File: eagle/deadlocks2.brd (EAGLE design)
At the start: 18 parts, among them J1 6_PIN_SERIAL_CABLEPTH, U1 328P

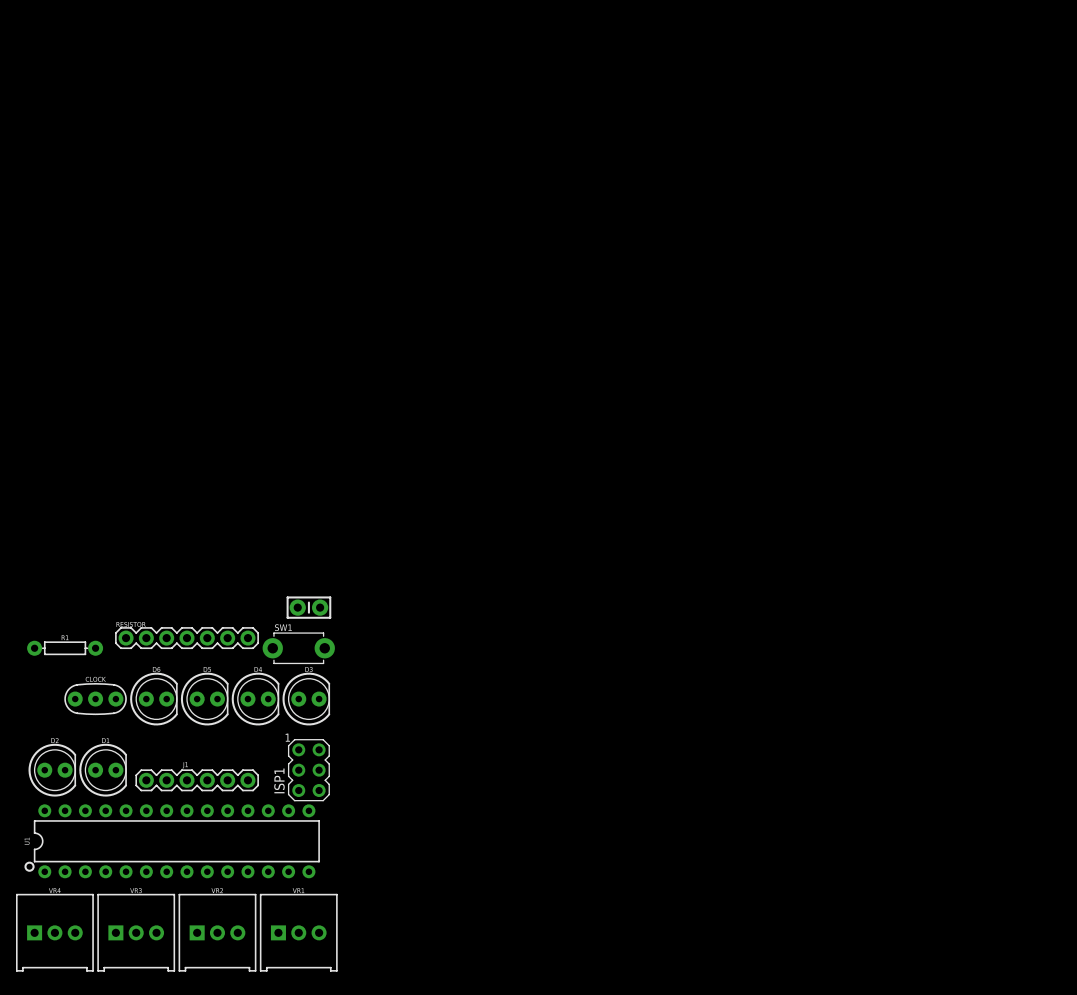
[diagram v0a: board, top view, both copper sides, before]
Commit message: Updates to BOM, board design, and datasheets.
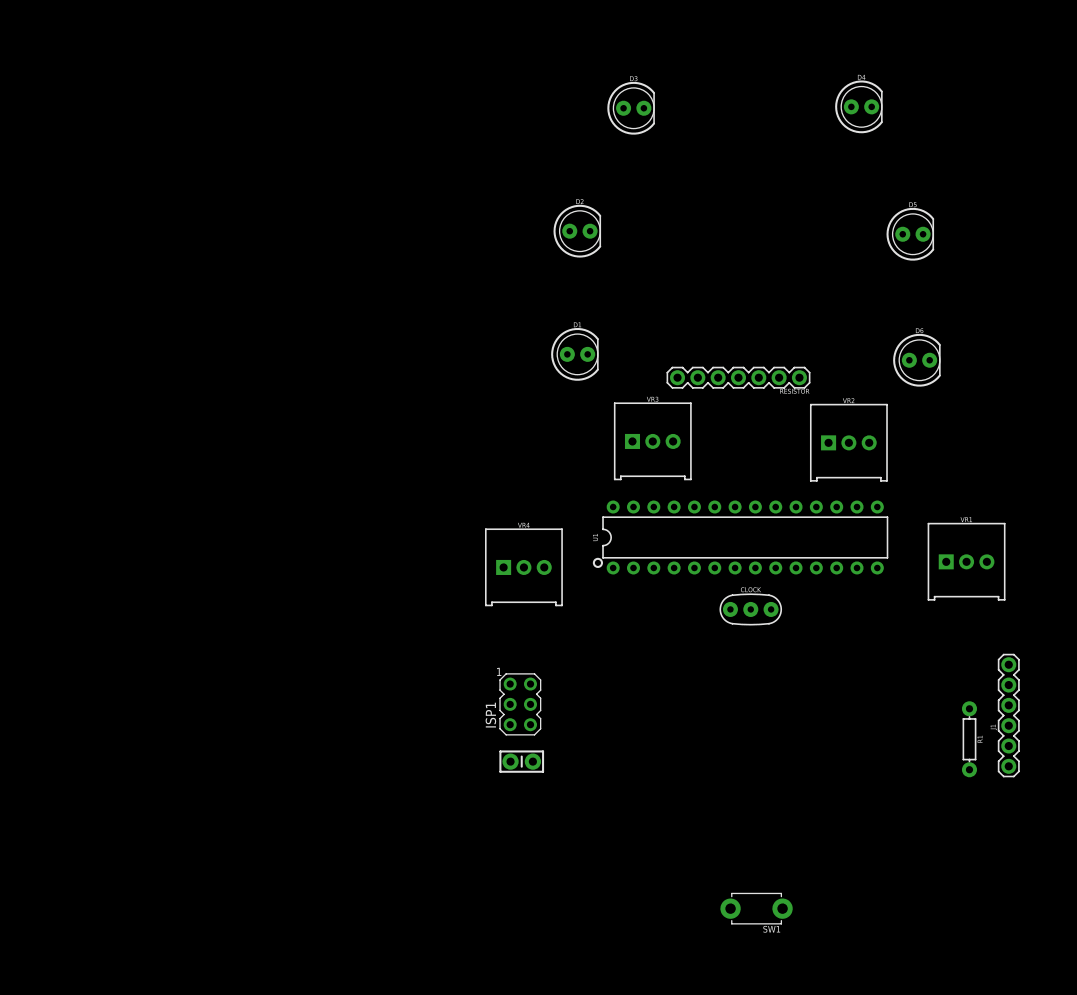
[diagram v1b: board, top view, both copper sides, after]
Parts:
- moved R1 113.6 mm to (66.1, 30.5), turned to 270 degrees
- moved J1 107.8 mm to (71.0, 27.1), turned to 90 degrees
- moved D4 105.7 mm to (52.6, 109.6)
- moved D5 105.6 mm to (59.0, 93.7)
- moved D6 104.4 mm to (59.8, 77.9)
- moved VR2 99.9 mm to (51.0, 67.6)
- moved VR1 95.5 mm to (65.7, 52.7)
- moved D2 94.1 mm to (17.4, 94.0)
- moved RESISTOR 90.2 mm to (44.8, 75.7), turned to 180 degrees
- moved VR3 89.1 mm to (26.5, 67.8)
- moved D3 84.3 mm to (24.1, 109.4)
- moved CLOCK 82.7 mm to (38.7, 46.8)
- moved U1 80.6 mm to (38.0, 55.8)
- moved D1 78.6 mm to (17.1, 78.6)
- moved VR4 74.3 mm to (10.4, 52.0)
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
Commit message: Updated board
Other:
- board outline added: 78.4 x 120.2 mm
- board text removed: "/home/thedevilsvoice/workspace/dead10c5_2018/art/DE:AD:10:C5-2.bmp"
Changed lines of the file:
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@@
 <layer number="27" name="tValues" color="7" fill="1" visible="yes" active="yes"/>
 <layer number="28" name="bValues" color="7" fill="1" visible="yes" active="yes"/>
-<layer number="29" name="tStop" color="7" fill="3" visible="no" active="yes"/>
-<layer number="30" name="bStop" color="7" fill="6" visible="no" active="yes"/>
-<layer number="31" name="tCream" color="7" fill="4" visible="no" active="yes"/>
-<layer number="32" name="bCream" color="7" fill="5" visible="no" active="yes"/>
-<layer number="33" name="tFinish" color="6" fill="3" visible="no" active="yes"/>
-<layer number="34" name="bFinish" color="6" fill="6" visible="no" active="yes"/>
-<layer number="35" name="tGlue" color="7" fill="4" visible="no" active="yes"/>
-<layer number="36" name="bGlue" color="7" fill="5" visible="no" active="yes"/>
-<layer number="37" name="tTest" color="7" fill="1" visible="no" active="yes"/>
-<layer number="38" name="bTest" color="7" fill="1" visible="no" active="yes"/>
+<layer number="29" name="tStop" color="7" fill="3" visible="yes" active="yes"/>
+<layer number="30" name="bStop" color="7" fill="6" visible="yes" active="yes"/>
+<layer number="31" name="tCream" color="7" fill="4" visible="yes" active="yes"/>
+<layer number="32" name="bCream" color="7" fill="5" visible="yes" active="yes"/>
+<layer number="33" name="tFinish" color="6" fill="3" visible="yes" active="yes"/>
+<layer number="34" name="bFinish" color="6" fill="6" visible="yes" active="yes"/>
+<layer number="35" name="tGlue" color="7" fill="4" visible="yes" active="yes"/>
+<layer number="36" name="bGlue" color="7" fill="5" visible="yes" active="yes"/>
+<layer number="37" name="tTest" color="7" fill="1" visible="yes" active="yes"/>
+<layer number="38" name="bTest" color="7" fill="1" visible="yes" active="yes"/>
 <layer number="39" name="tKeepout" color="4" fill="11" visible="yes" active="yes"/>
 <layer number="40" name="bKeepout" color="1" fill="11" visible="yes" active="yes"/>
@@
 <layer number="42" name="bRestrict" color="1" fill="10" visible="yes" active="yes"/>
 <layer number="43" name="vRestrict" color="2" fill="10" visible="yes" active="yes"/>
-<layer number="44" name="Drills" color="7" fill="1" visible="no" active="yes"/>
-<layer number="45" name="Holes" color="7" fill="1" visible="no" active="yes"/>
-<layer number="46" name="Milling" color="3" fill="1" visible="no" active="yes"/>
-<layer number="47" name="Measures" color="7" fill="1" visible="no" active="yes"/>
+<layer number="44" name="Drills" color="7" fill="1" visible="yes" active="yes"/>
+<layer number="45" name="Holes" color="7" fill="1" visible="yes" active="yes"/>
+<layer number="46" name="Milling" color="3" fill="1" visible="yes" active="yes"/>
+<layer number="47" name="Measures" color="7" fill="1" visible="yes" active="yes"/>
 <layer number="48" name="Document" color="7" fill="1" visible="yes" active="yes"/>
 <layer number="49" name="Reference" color="7" fill="1" visible="yes" active="yes"/>
@@
 <rectangle x1="38.9375" y1="119.6125" x2="39.1125" y2="119.7875" layer="200"/>
 <rectangle x1="36.3125" y1="119.7875" x2="37.7125" y2="119.9625" layer="200"/>
-<text x="0" y="-0.875" size="0.35" layer="200" font="vector">/home/thedevilsvoice/workspace/dead10c5_2018/art/DE:AD:10:C5-2.bmp</text>
 <dimension x1="37.45" y1="119.875" x2="37.275" y2="0.875" x3="83.56394375" y3="60.30705625" textsize="3.81" layer="49" unit="inch" visible="yes"/>
 <dimension x1="0.2625" y1="40.6875" x2="76.825" y2="40.775" x3="38.45034375" y3="122.462340625" textsize="2.1844" layer="49" unit="inch" visible="yes"/>
+<wire x1="22.75" y1="76.3" x2="54.075" y2="76.125" width="0.1524" layer="20" curve="-47.406574"/>
+<wire x1="22.75" y1="76.475" x2="23.275" y2="93.45" width="0.1524" layer="20"/>
+<wire x1="53.9" y1="76.3" x2="53.2" y2="93.975" width="0.1524" layer="20"/>
+<wire x1="23.275" y1="93.45" x2="53.2" y2="93.975" width="0.1524" layer="20" curve="-180"/>
+<wire x1="11.55" y1="95.025" x2="65.1" y2="92.75" width="0.1524" layer="20" curve="-180.768921"/>
+<wire x1="11.55" y1="95.025" x2="11.025" y2="68.25" width="0.1524" layer="20"/>
+<wire x1="65.1" y1="92.925" x2="65.625" y2="67.725" width="0.1524" layer="20"/>
+<wire x1="65.625" y1="67.9" x2="11.025" y2="68.25" width="0.1524" layer="20" curve="-271.792094"/>
 </plain>
 <attributes>
